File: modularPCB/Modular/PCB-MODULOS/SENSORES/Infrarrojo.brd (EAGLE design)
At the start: 35 x 20 mm, 9 parts

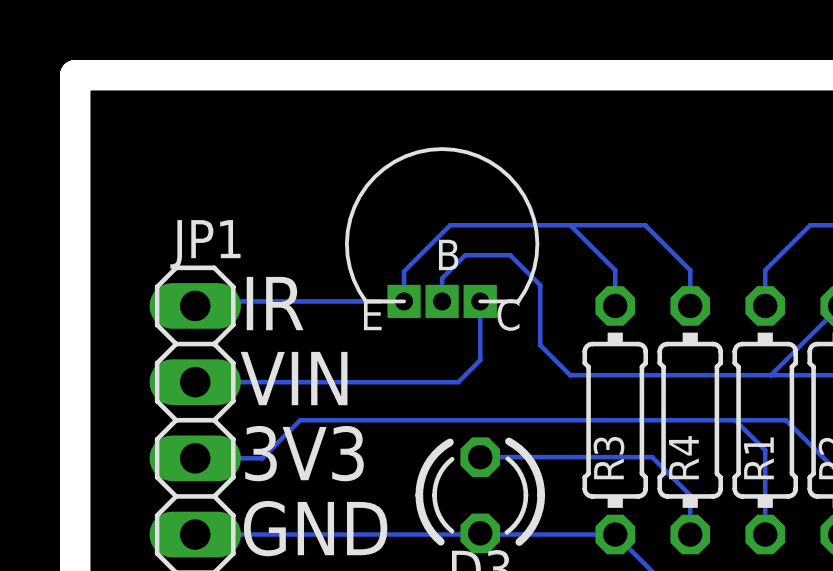
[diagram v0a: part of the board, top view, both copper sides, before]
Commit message: Corrección de errores en pcbs
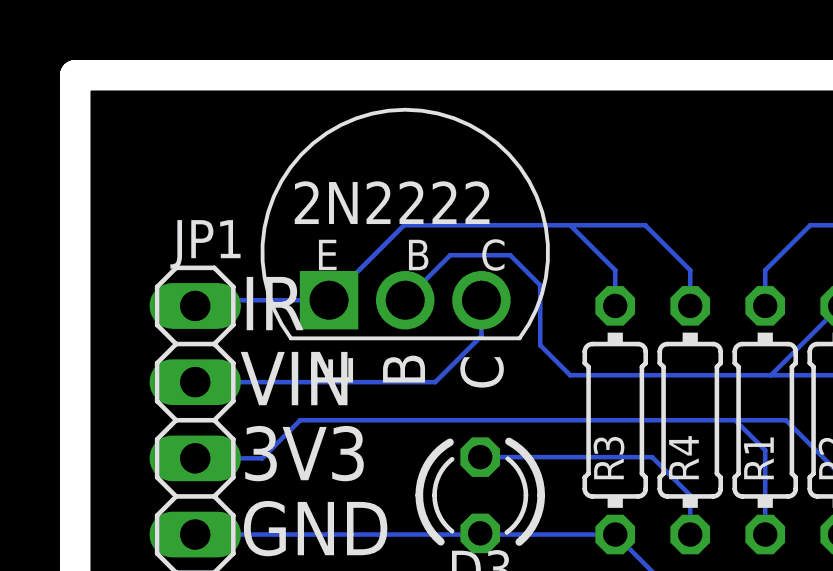
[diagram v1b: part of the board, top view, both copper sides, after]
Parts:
- removed U$6: 2N2222, MODULAR:2N2222
- added U$1: 2N2222, MODULAR:2N2222
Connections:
- net N$30: now also U$1.B; no longer U$6.B
- net PULSO-INFRA: now also U$1.E; no longer U$6.E
- net VIN: now also U$1.C; no longer U$6.C
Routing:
- net N$30: track 25.6 -> 26.4 mm
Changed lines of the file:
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@@
 <text x="5.5" y="6.5" size="1.778" layer="21">3V3</text>
 <text x="5.5" y="4" size="1.778" layer="21">GND</text>
-<text x="9.5" y="11.5" size="1.016" layer="21">E</text>
-<text x="12" y="13.5" size="1.016" layer="21">B</text>
-<text x="14" y="11.5" size="1.016" layer="21">C</text>
+<text x="8" y="13.5" size="1.016" layer="21">E</text>
+<text x="11" y="13.5" size="1.016" layer="21">B</text>
+<text x="13.5" y="13.5" size="1.016" layer="21">C</text>
 <dimension x1="35" y1="0" x2="35" y2="20" x3="38.5" y3="10" textsize="1.778" layer="48"/>
 <dimension x1="35" y1="20" x2="0" y2="20" x3="17.5" y3="23" textsize="1.778" layer="48"/>
@@
 <attribute name="VALUE" x="28.595" y="8.151" size="1.27" layer="27" ratio="10" rot="R180"/>
 </element>
-<element name="U$6" library="MODULAR" package="2N2222" value="2N2222" x="13.5" y="15" smashed="yes" rot="R90"/>
+<element name="U$1" library="MODULAR" package="2N2222" value="2N2222" x="11" y="12.5" smashed="yes"/>
 </elements>
 <signals>
@@
 </signal>
 <signal name="VIN">
-<contactref element="U$6" pad="C"/>
 <contactref element="JP1" pad="3"/>
-<wire x1="4" y1="9.77" x2="12.77" y2="9.77" width="0.1524" layer="16"/>
-<wire x1="12.77" y1="9.77" x2="13.5" y2="10.5" width="0.1524" layer="16"/>
-<wire x1="13.5" y1="10.5" x2="13.5" y2="12.46" width="0.1524" layer="16"/>
+<wire x1="4" y1="9.77" x2="12" y2="9.77" width="0.1524" layer="16"/>
+<contactref element="U$1" pad="C"/>
+<wire x1="13.54" y1="12.5" x2="13.54" y2="11.31" width="0.1524" layer="16"/>
+<wire x1="13.54" y1="11.31" x2="12" y2="9.77" width="0.1524" layer="16"/>
 </signal>
 <signal name="GND">
@@
 <contactref element="R2" pad="1"/>
 <contactref element="D2R" pad="K"/>
-<contactref element="U$6" pad="B"/>
-<wire x1="12.23" y1="12.46" x2="12.23" y2="13.23" width="0.1524" layer="16"/>
-<wire x1="12.23" y1="13.23" x2="13" y2="14" width="0.1524" layer="16"/>
-<wire x1="13" y1="14" x2="14.5" y2="14" width="0.1524" layer="16"/>
 <wire x1="15.5" y1="13" x2="15.5" y2="11" width="0.1524" layer="16"/>
 <wire x1="15.5" y1="11" x2="16.5" y2="10" width="0.1524" layer="16"/>
-<wire x1="14.5" y1="14" x2="15.5" y2="13" width="0.1524" layer="16"/>
+<wire x1="15.5" y1="13" x2="14.5" y2="14" width="0.1524" layer="16"/>
 <wire x1="23.19" y1="10" x2="25.5" y2="12.31" width="0.1524" layer="16"/>
 <wire x1="16.5" y1="10" x2="23.19" y2="10" width="0.1524" layer="16"/>
 <wire x1="29.23" y1="6.5" x2="25.73" y2="10" width="0.1524" layer="16"/>
 <wire x1="25.73" y1="10" x2="23.19" y2="10" width="0.1524" layer="16"/>
+<contactref element="U$1" pad="B"/>
+<wire x1="12.5" y1="14" x2="11" y2="12.5" width="0.1524" layer="16"/>
+<wire x1="14.5" y1="14" x2="12.5" y2="14" width="0.1524" layer="16"/>
 </signal>
 <signal name="N$31">
@@
 <signal name="PULSO-INFRA">
 <contactref element="R3" pad="1"/>
-<contactref element="U$6" pad="E"/>
 <contactref element="R4" pad="2"/>
 <contactref element="JP1" pad="4"/>
 <wire x1="4" y1="12.31" x2="4.15" y2="12.46" width="0.1524" layer="16"/>
-<wire x1="4.15" y1="12.46" x2="10.96" y2="12.46" width="0.1524" layer="16"/>
-<wire x1="10.96" y1="12.46" x2="10.96" y2="13.46" width="0.1524" layer="16"/>
-<wire x1="10.96" y1="13.46" x2="12.5" y2="15" width="0.1524" layer="16"/>
-<wire x1="12.5" y1="15" x2="16.5" y2="15" width="0.1524" layer="16"/>
 <wire x1="18" y1="13.5" x2="16.5" y2="15" width="0.1524" layer="16"/>
 <wire x1="18" y1="13.5" x2="18" y2="12.31" width="0.1524" layer="16"/>
@@
 <wire x1="19" y1="15" x2="20.5" y2="13.5" width="0.1524" layer="16"/>
 <wire x1="20.5" y1="13.5" x2="20.5" y2="12.31" width="0.1524" layer="16"/>
+<contactref element="U$1" pad="E"/>
+<wire x1="10.96" y1="15" x2="8.46" y2="12.5" width="0.1524" layer="16"/>
+<wire x1="16.5" y1="15" x2="10.96" y2="15" width="0.1524" layer="16"/>
+<wire x1="4" y1="12.31" x2="4.19" y2="12.5" width="0.1524" layer="16"/>
+<wire x1="4.19" y1="12.5" x2="8.46" y2="12.5" width="0.1524" layer="16"/>
 </signal>
 </signals>

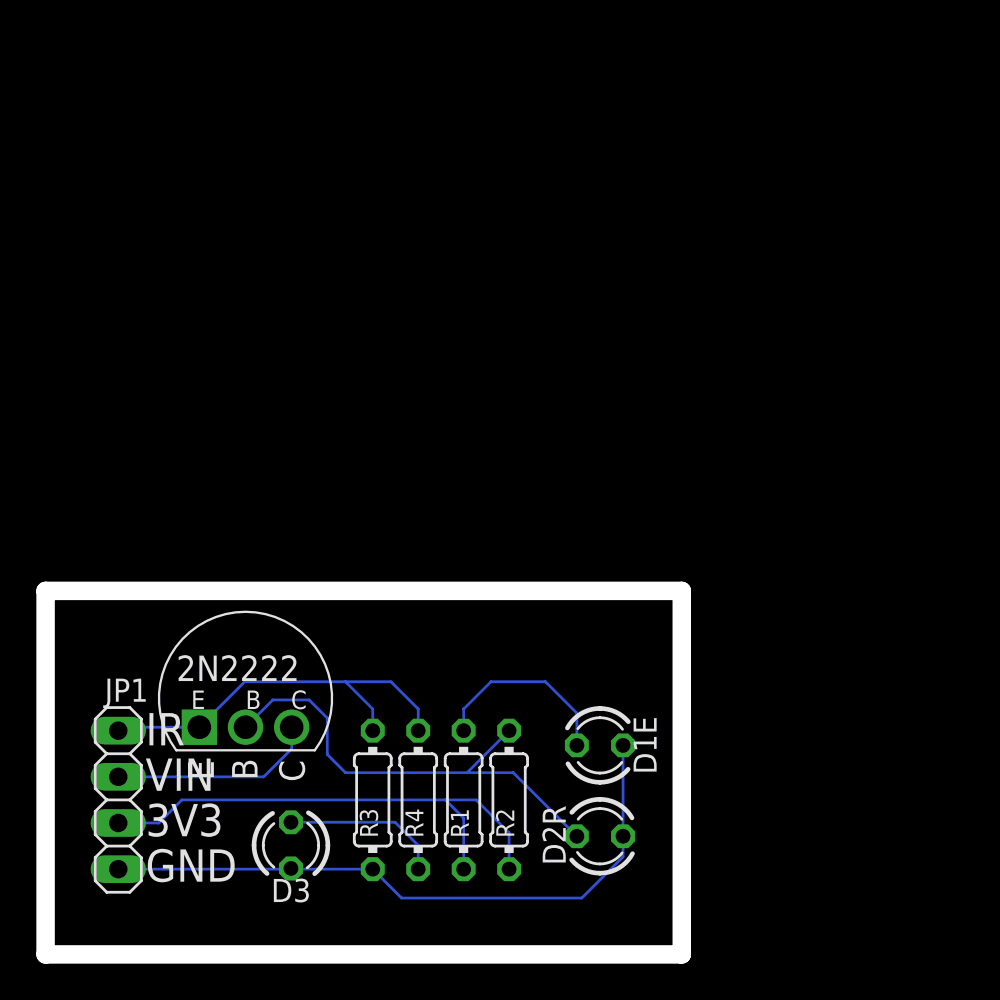
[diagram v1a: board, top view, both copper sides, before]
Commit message: Se agregaron brd de la ultima actualización
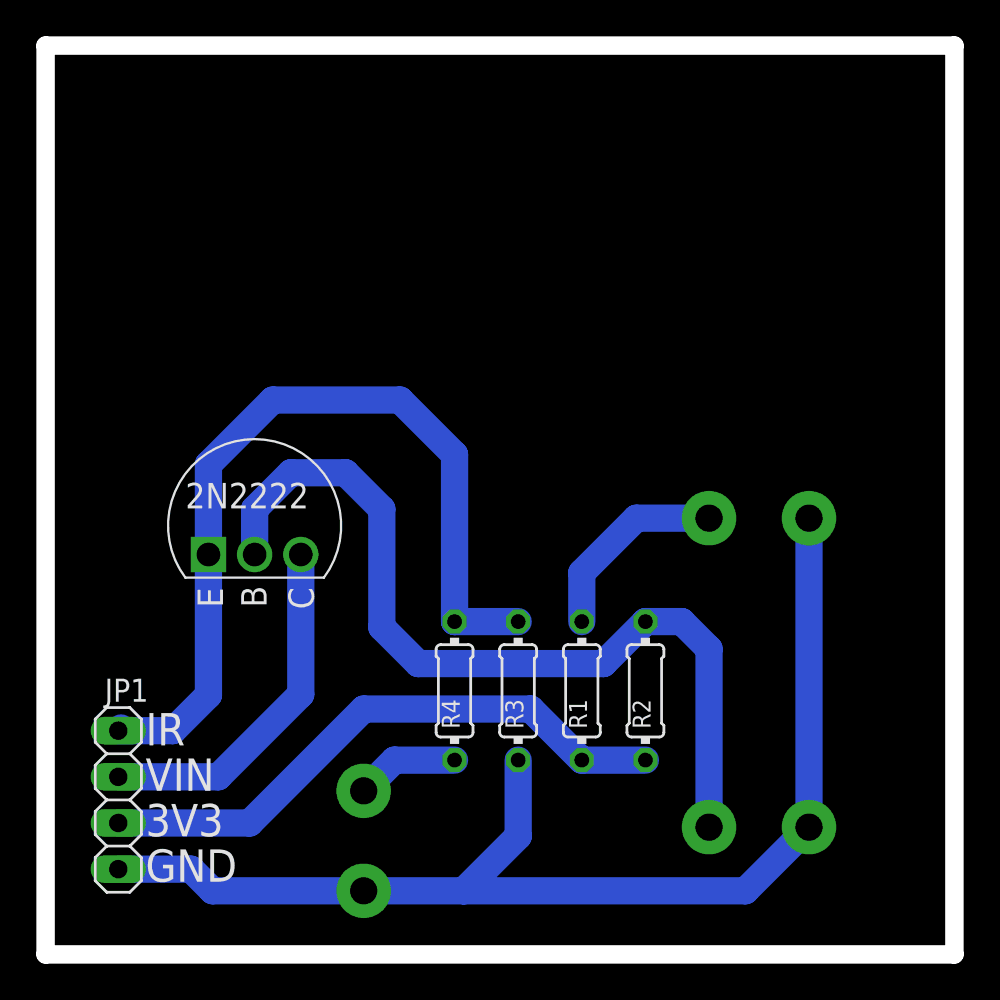
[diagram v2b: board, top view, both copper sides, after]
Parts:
- removed D1E, D2R, D3: (no value), led:LED3MM
- moved R3 10.0 mm to (26.0, 14.5)
- moved R2 9.60 mm to (33.0, 14.5)
- moved U$1 9.51 mm to (11.5, 22.0)
- moved R1 8.85 mm to (29.5, 14.5)
- moved R4 6.32 mm to (22.5, 14.5)
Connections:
- removed net N$20: D1E.A, R1.1
- removed net N$30: D2R.K, R2.1, U$1.B
- removed net N$31: D3.A, R4.1
- new net EMISOR: R1.1
- new net LED: R4.1
- new net RECEPTOR: R2.1, U$1.B
- net GND: no longer D1E.K, D2R.A, D3.K
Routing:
- net RECEPTOR: track 0.00 -> 47.9 mm, vias 0 -> 1
- net GND: track 35.5 -> 65.4 mm, vias 0 -> 3
- net N$30: track 26.4 -> 0.00 mm
- net PULSO-INFRA: track 22.9 -> 47.6 mm
- net EMISOR: track 0.00 -> 10.9 mm, vias 0 -> 1
- net N$20: track 10.5 -> 0.00 mm
- net N$31: track 8.84 -> 0.00 mm
- net VIN: track 11.4 -> 19.6 mm
- net LED: track 0.00 -> 5.70 mm, vias 0 -> 1
- net 3V3: track 29.0 -> 32.8 mm
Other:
- board size 35 x 20 mm -> 50 x 50 mm
- board text removed: "B"
- board text removed: "C"
- board text removed: "E"
